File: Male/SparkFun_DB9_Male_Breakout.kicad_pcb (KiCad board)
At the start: 4 copper layers, 22.9 x 31 mm, 23 parts, among them J1 DE9-Male, J2 Conn_01x09

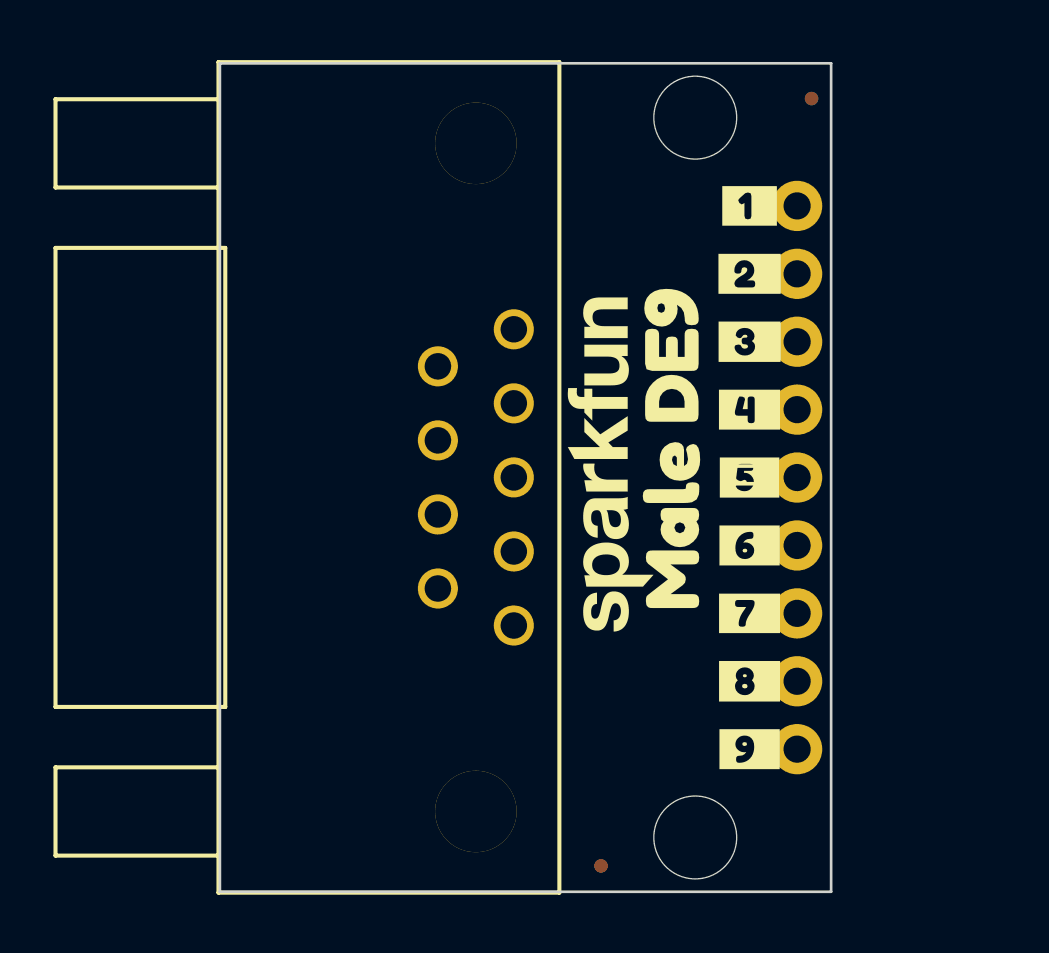
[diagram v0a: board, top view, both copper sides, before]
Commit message: Adds a male footprint for the DB9 and updates the affected board
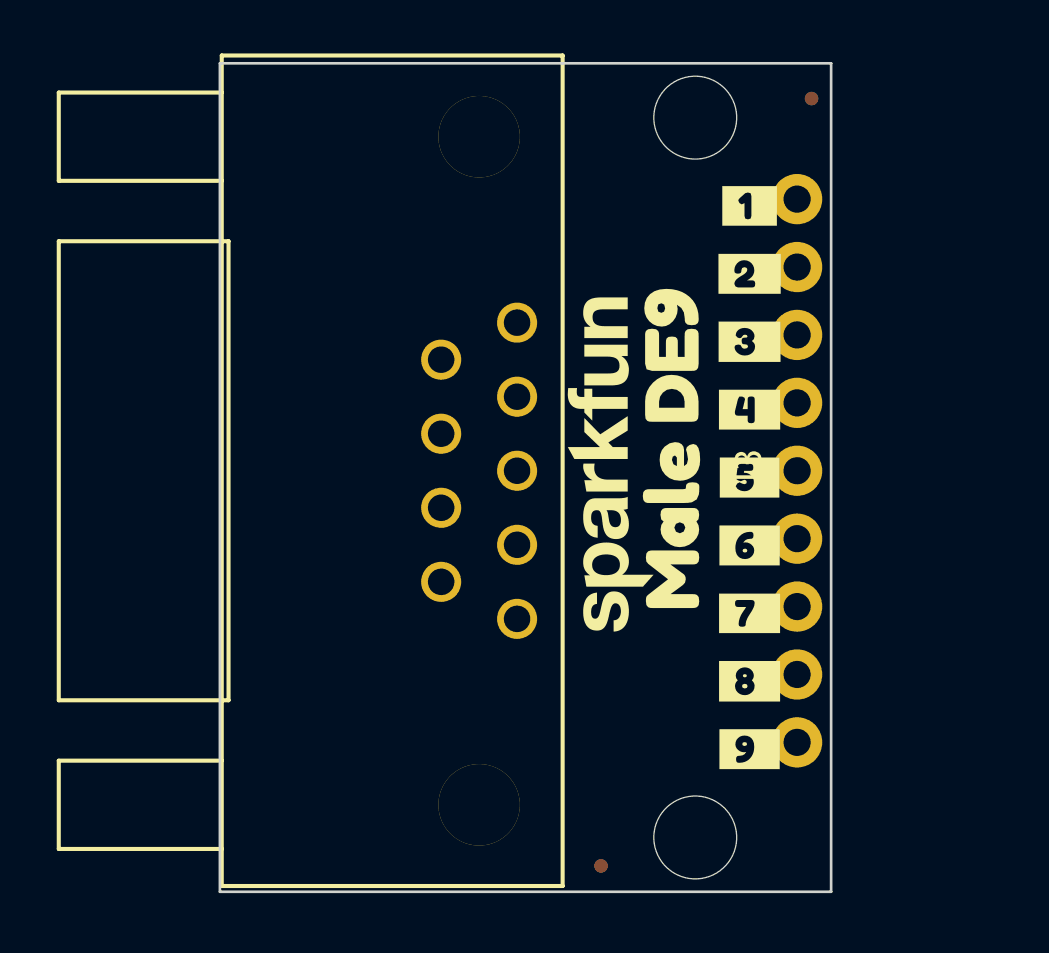
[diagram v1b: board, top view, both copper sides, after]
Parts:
- removed J1: DE9-Male, DE9-Footprint:DB9
- added J3: DE9-Male, DE9-Footprint:DB9, F.Cu at (109.7, 108.5)
- moved J2 0.25 mm to (131.1, 98.3)

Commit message: Adds some underbars to numbers, adds silk to bottom side on male DB9
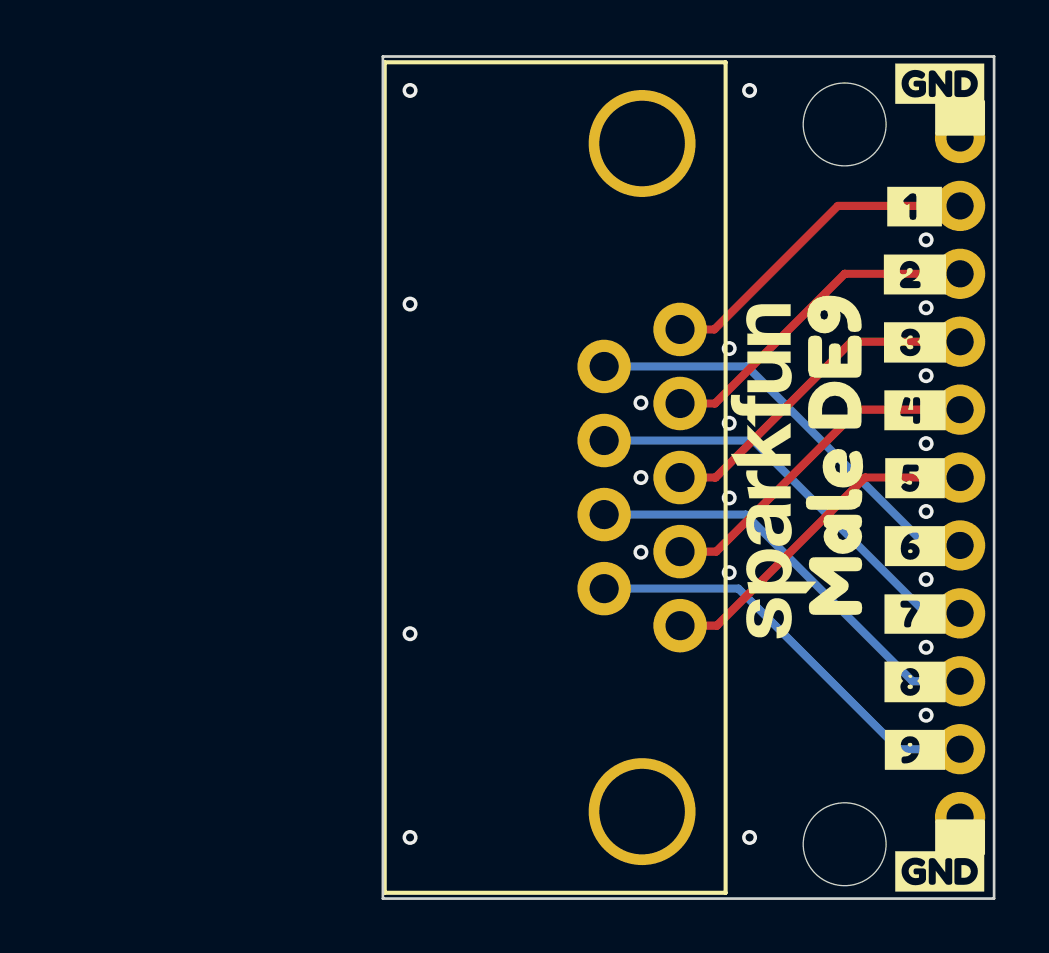
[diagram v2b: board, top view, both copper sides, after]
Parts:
- removed FID1, FID2, FID3, FID4: Fiducial_0.5mm, SparkFun-Aesthetic:Fiducial_0.5mm_Mask1mm
- removed the G*** at (113.8, 98.8)
- added G***: Flame, SparkFun-Aesthetic:SparkFun_Flame_6mm, B.Cu at (119.6, 97.1)
- added J1: Conn_01x01, SparkFun-Connector:1x01, F.Cu at (137.2, 96.0)
- added J4: Conn_01x01, SparkFun-Connector:1x01, F.Cu at (137.2, 121.4)
- added kibuzzard-67DDA384: G***, kibuzzard-67DDA384, B.Cu at (135.5, 98.6)
- added kibuzzard-67DDA391: G***, kibuzzard-67DDA391, B.Cu at (135.5, 101.1)
- added kibuzzard-67DDA399: G***, kibuzzard-67DDA399, B.Cu at (135.5, 103.7)
- added kibuzzard-67DDA3A2: G***, kibuzzard-67DDA3A2, B.Cu at (135.5, 106.2)
- added kibuzzard-67DDA3AA: G***, kibuzzard-67DDA3AA, B.Cu at (135.5, 108.7)
- added kibuzzard-67DDA3B0: G***, kibuzzard-67DDA3B0, B.Cu at (135.5, 111.3)
- added kibuzzard-67DDA3B8: G***, kibuzzard-67DDA3B8, B.Cu at (135.5, 113.8)
- added kibuzzard-67DDA3D5: G***, kibuzzard-67DDA3D5, B.Cu at (135.5, 116.4)
- added kibuzzard-67DDA3E0: G***, kibuzzard-67DDA3E0, B.Cu at (135.5, 118.9)
- added kibuzzard-67DDBC91: G***, kibuzzard-67DDBC91, F.Cu at (136.4, 123.4)
- added kibuzzard-67DDBC91: G***, kibuzzard-67DDBC91, F.Cu at (136.4, 94.0)
- added kibuzzard-67DDBC91: G***, kibuzzard-67DDBC91, B.Cu at (136.4, 94.0)
- added kibuzzard-67DDBC91: G***, kibuzzard-67DDBC91, B.Cu at (136.4, 123.4)
- added kibuzzard-67DDBDB0: G***, kibuzzard-67DDBDB0, B.Cu at (128.7, 105.9)
- added kibuzzard-67DDBDCA: G***, kibuzzard-67DDBDCA, B.Cu at (128.7, 103.1)
- added kibuzzard-67DDBDCE: G***, kibuzzard-67DDBDCE, B.Cu at (128.7, 108.8)
- added kibuzzard-67DDBDD2: G***, kibuzzard-67DDBDD2, B.Cu at (128.7, 111.6)
- added kibuzzard-67DDBDD7: G***, kibuzzard-67DDBDD7, B.Cu at (128.7, 114.3)
- added kibuzzard-67DDBDDC: G***, kibuzzard-67DDBDDC, B.Cu at (121.9, 113.0)
- added kibuzzard-67DDBDF0: G***, kibuzzard-67DDBDF0, B.Cu at (121.8, 107.4)
- added kibuzzard-67DDBDF6: G***, kibuzzard-67DDBDF6, B.Cu at (121.9, 110.2)
- added kibuzzard-67DDBDFC: G***, kibuzzard-67DDBDFC, B.Cu at (121.8, 104.4)
- moved kibuzzard-67D496B8 6.19 mm to (135.5, 101.1)
- moved kibuzzard-67D496C7 6.19 mm to (135.5, 103.7)
- moved kibuzzard-67D496CD 6.19 mm to (135.5, 106.2)
- moved kibuzzard-67D496D5 6.19 mm to (135.5, 108.7)
- moved kibuzzard-67D496DD 6.19 mm to (135.5, 111.3)
- moved kibuzzard-67D496E4 6.19 mm to (135.5, 113.8)
- moved kibuzzard-67D496EA 6.19 mm to (135.5, 116.4)
- moved kibuzzard-67D496F6 6.19 mm to (135.5, 118.9)
- moved kibuzzard-67D49687 6.17 mm to (135.5, 98.6)
- moved kibuzzard-67D49838 6.10 mm to (132.5, 104.4)
- moved kibuzzard-67DB37C8 6.10 mm to (132.5, 110.7)
- moved J2 6.10 mm to (137.2, 98.6)
- moved J3 6.10 mm to (115.8, 108.7)
- moved G*** 6.10 mm to (129.9, 108.8)
- moved Ref** 6.10 mm to (119.4, 121.2)
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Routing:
- net /6: track 0.00 -> 16.1 mm
- net /7: track 0.00 -> 16.0 mm
- net /8: track 0.00 -> 15.9 mm
- net /9: track 0.00 -> 15.8 mm
- net /5: track 0.00 -> 12.8 mm
- net /4: track 0.00 -> 12.7 mm
- net /3: track 0.00 -> 12.6 mm
- net /2: track 0.00 -> 12.5 mm
- net /1: track 0.00 -> 12.4 mm
- net GND: vias 0 -> 21
- added copper zone on B.Cu, net GND
- added copper zone on F.Cu, net GND
- removed copper zone on B.Cu, net /9
- removed copper zone on F.Cu, net /9
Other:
- board size 22.9 x 31 mm -> 22.9 x 31.5 mm
